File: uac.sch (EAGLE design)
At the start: 221 parts, among them Q1 2N7002CK4SST, Q2 2N7002CK4SST, Q3 2N7002CK4SST, Q4 2N7002CK4SST, Q5 2N7002CK4SST, U1 MCP73833-FCI/UN, U2 ADXL345, Y1 RESONATORSMD

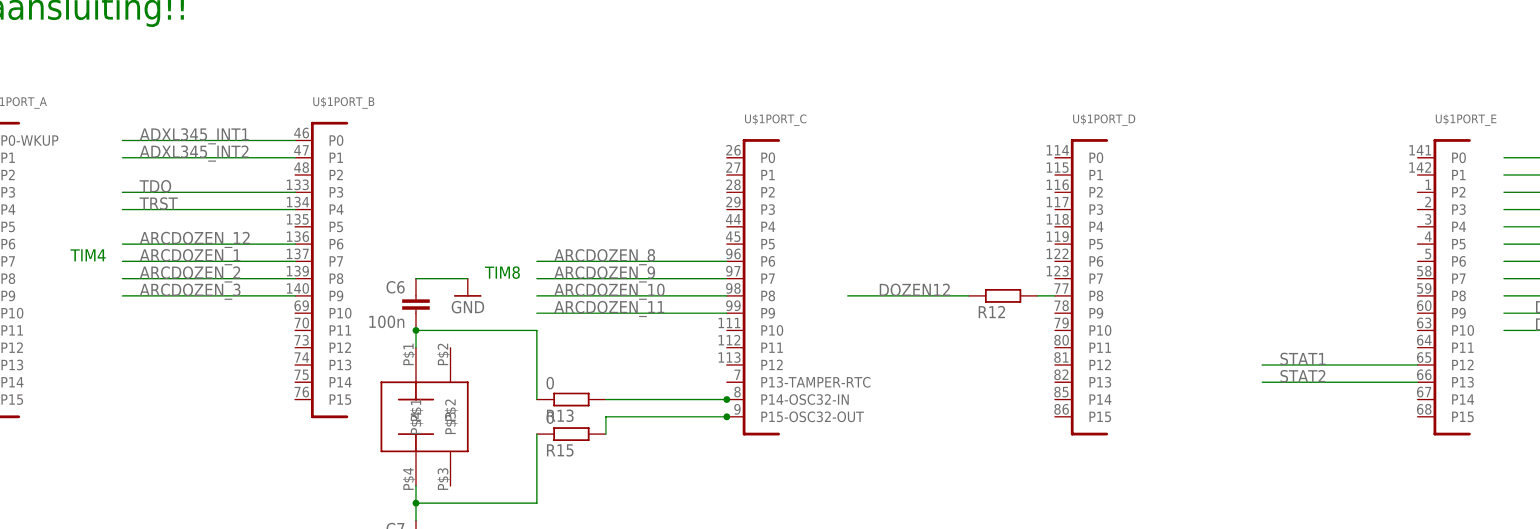
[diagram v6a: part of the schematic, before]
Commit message: placed wake up light
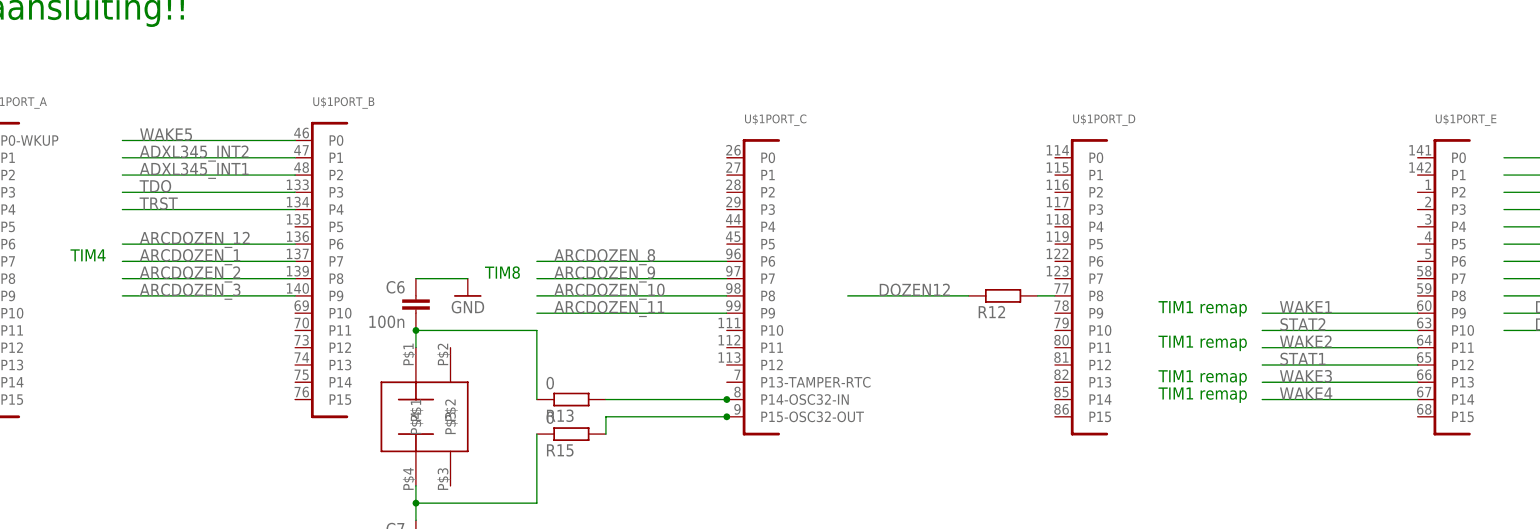
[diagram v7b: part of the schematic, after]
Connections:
- net ADXL345_INT1: now also U$1PORT_B.P2; no longer U$1PORT_B.P0
- net STAT2: now also U$1PORT_E.P10; no longer U$1PORT_E.P13
- net WAKE1: now also U$1PORT_E.P9
- net WAKE2: now also U$1PORT_E.P11
- net WAKE3: now also U$1PORT_E.P13
- net WAKE4: now also U$1PORT_E.P14
- net WAKE5: now also U$1PORT_B.P0
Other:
- note added: "TIM1 remap"

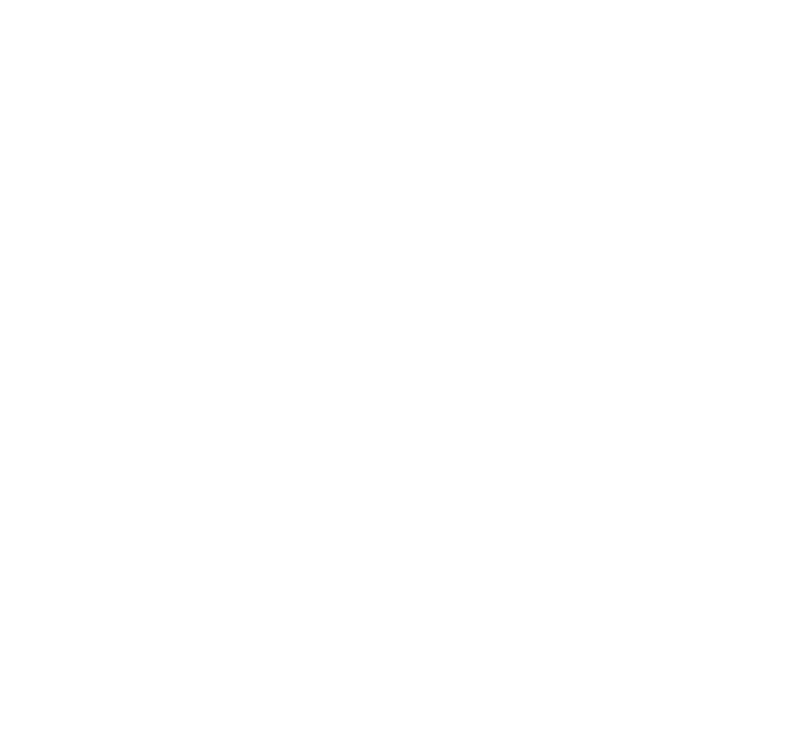
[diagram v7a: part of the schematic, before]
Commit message: Added cc3000 wifi
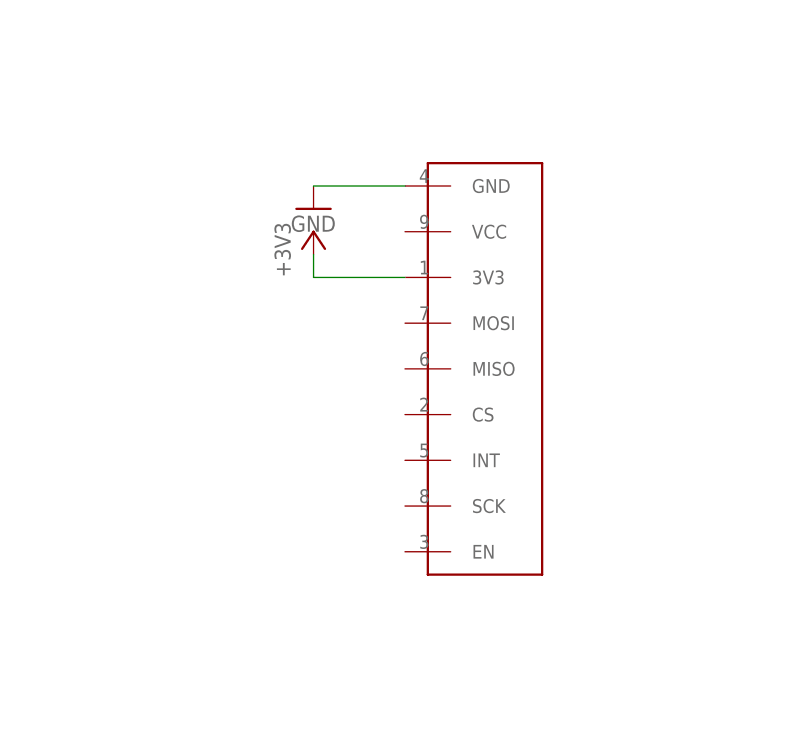
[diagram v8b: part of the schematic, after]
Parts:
- added U$9: CC3000, timearc:CC3000
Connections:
- net +3V3: now also U$9.3V3
- net GND: now also U$9.GND
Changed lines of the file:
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@@
 <part name="R26" library="Custom components" deviceset="R-EU_" device="R0603" value="200"/>
 <part name="P+6" library="Custom components" deviceset="+5V" device=""/>
+<part name="U$9" library="timearc" deviceset="CC3000" device=""/>
+<part name="GND20" library="supply1" deviceset="GND" device=""/>
+<part name="+3V8" library="Custom components" deviceset="+3V3" device=""/>
 </parts>
 <sheets>
@@
 <instance part="R26" gate="G$1" x="439.42" y="177.8" rot="MR180"/>
 <instance part="P+6" gate="1" x="447.04" y="182.88"/>
+<instance part="U$9" gate="G$1" x="736.6" y="215.9"/>
+<instance part="GND20" gate="1" x="718.82" y="226.06"/>
+<instance part="+3V8" gate="G$1" x="718.82" y="223.52"/>
 </instances>
 <busses>
@@
 <wire x1="414.02" y1="172.72" x2="414.02" y2="170.18" width="0.1524" layer="91"/>
 </segment>
+<segment>
+<pinref part="GND20" gate="1" pin="GND"/>
+<pinref part="U$9" gate="G$1" pin="GND"/>
+<wire x1="718.82" y1="228.6" x2="728.98" y2="228.6" width="0.1524" layer="91"/>
+</segment>
 </net>
 <net name="+3V3" class="0">
@@
 <junction x="406.4" y="66.04"/>
 </segment>
-</net>
+<segment>
+<pinref part="U$9" gate="G$1" pin="3V3"/>
+<pinref part="+3V8" gate="G$1" pin="+3V3"/>
+<wire x1="728.98" y1="218.44" x2="718.82" y2="218.44" width="0.1524" layer="91"/>
+<wire x1="718.82" y1="218.44" x2="718.82" y2="220.98" width="0.1524" layer="91"/>
+</segment>
+</net>
